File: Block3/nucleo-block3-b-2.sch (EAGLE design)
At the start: 91 parts, among them IC1 TL331, J4 MODJACK6P6C-MJ3245-66-0CONN_M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, J5 MODJACK6P6C-MJ3245-66-0CONN_M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, Q1 NPN-23, Q2 BSS123, Q3 BSS84, U1 TC4428, U2 TC4428, U3 TC4428

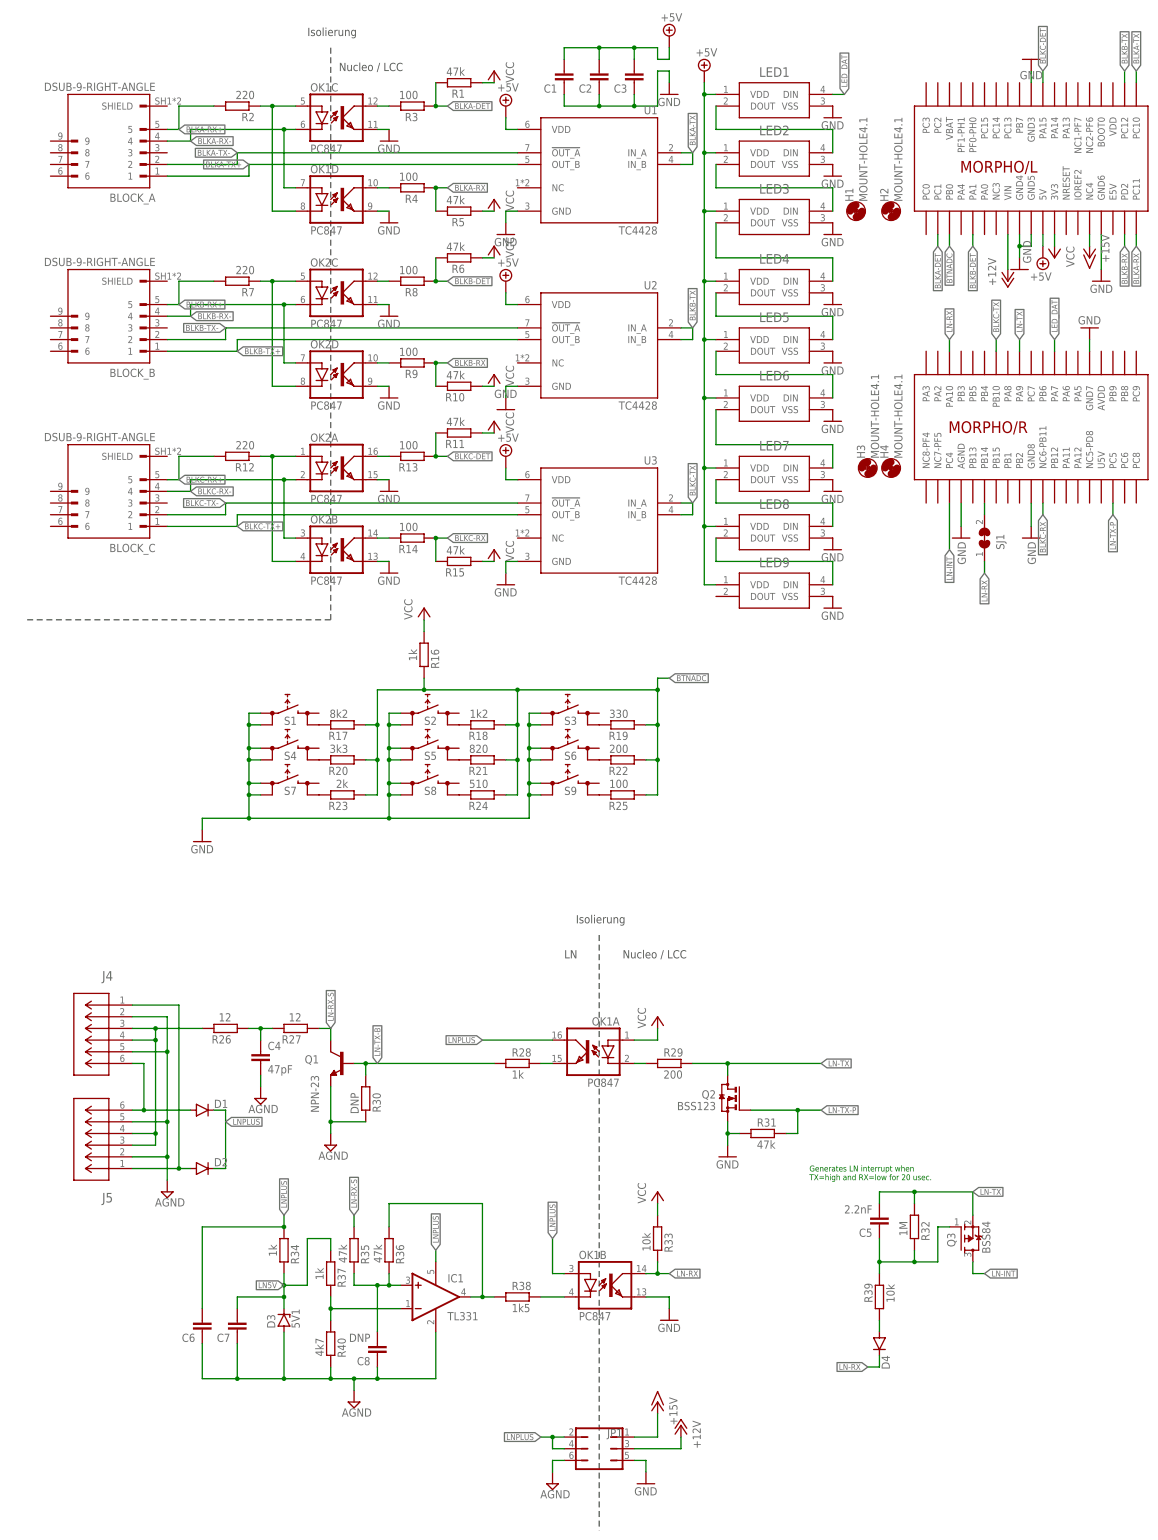
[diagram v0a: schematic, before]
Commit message: - adds a small TH pin "alignment hole" to the lib - fixes the DB-9 connector's pin order - updates the loconet-block3 board for rev B.
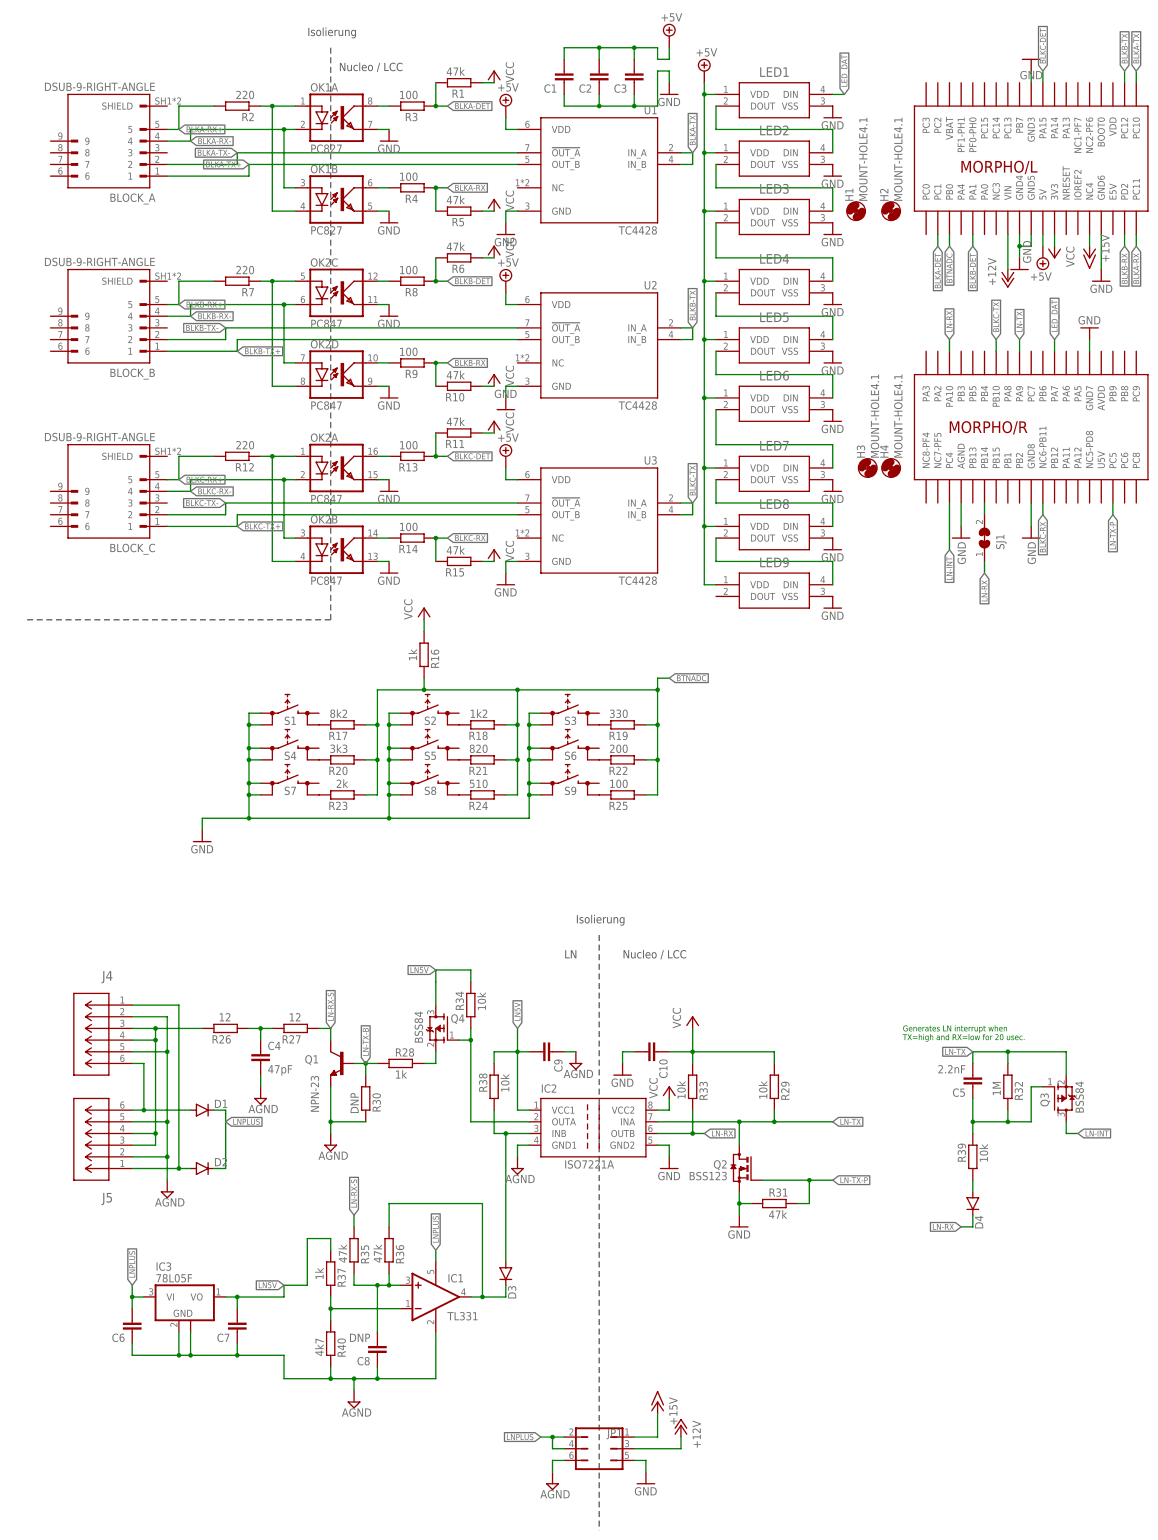
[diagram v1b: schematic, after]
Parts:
- added C10, C9: (no value), rcl:C-EUC0603
- added IC2: ISO7221A, texas:ISO7221A
- added IC3: 78L05F, linear:78L05F
- added Q4: BSS84, eagleparts:BSS84
- D3: value 5V1 -> (none); device diode:ZENER-DIODESOD80C -> diode:DIODE-MINIMELF
- OK1: value PC847 -> PC827; device optocoupler:PC847 -> optocoupler:PC827
- R29: value 200 -> 10k
- R34: value 1k -> 10k
- R38: value 1k5 -> 10k
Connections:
- removed net N$38: OK1A.C, R29.1
- removed net N$39: OK1B.C, R38.2
- new net N$20: D3.A, IC2.INB, R38.1
- new net N$8: IC2.OUTA, Q4.G, R34.1
- net AGND: now also C9.1, IC2.GND1, IC3.GND, IC3.GND@1; no longer D3.A
- net BLKA-RX-: now also OK1A.C, OK1B.A; no longer OK1C.C, OK1D.A
- net GND: now also C10.2, IC2.GND2, OK1A.EMIT; no longer OK1C.EMIT, OK1D.EMIT
- net LN-RX: now also IC2.OUTB; no longer OK1B.COL
- net LN-TX: now also IC2.INA
- net LN5V: now also C9.2, IC2.VCC1, IC3.VO, Q4.D, R38.2; no longer D3.C
- net LNPLUS: now also IC3.VI; no longer OK1A.COL, OK1B.A, R34.1
- net N$11: now also Q4.S; no longer OK1A.EMIT
- net N$31: now also OK1A.A, OK1B.C; no longer OK1C.A, OK1D.C
- net N$36: now also D3.C; no longer R38.1
- net N$41: now also OK1A.COL; no longer OK1C.COL
- net N$42: now also OK1B.COL; no longer OK1D.COL
- net VCC: now also C10.1, IC2.VCC2, R29.1; no longer OK1A.A
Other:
- moved on the sheet: C5, C6, D4, OK1A, OK1B, Q2, Q3, R28, R29, R31, R32, R33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
